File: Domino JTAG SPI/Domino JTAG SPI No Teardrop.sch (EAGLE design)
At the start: 29 parts, among them J1 MH8-1, J2 MH10-1, J3 MH10-1, J4 MH2-1, J5 MH8-1, J6 MHRA7-2-0.1, SW1 IT-1124SMD, U1 SPI_FLASH

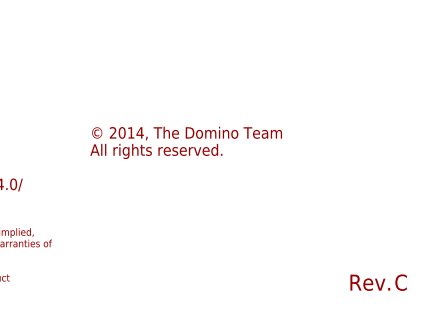
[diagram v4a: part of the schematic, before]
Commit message: Domino JTAG SPI Rev. D: changed silkscreen font ratio to 20%
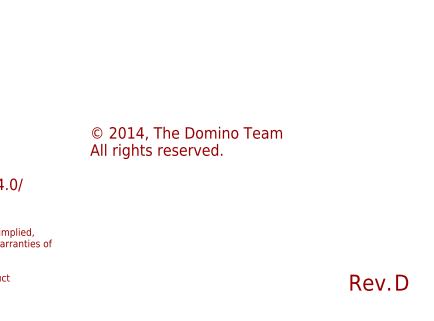
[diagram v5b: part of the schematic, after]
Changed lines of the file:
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@@
 <attribute name="DATABASE" value="./../Common/BOM/Domino_DB.txt"/>
 <attribute name="DRAWN" value="M.STEMPIN"/>
-<attribute name="REV" value="C"/>
+<attribute name="REV" value="D"/>
 </attributes>
 <variantdefs>
